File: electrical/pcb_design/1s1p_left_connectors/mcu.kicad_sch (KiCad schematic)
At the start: 14 parts, among them J17 STLINK_TagConnect_6, U1 BMI323, U2 BMI323, U4 STM32L452CEU6

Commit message: Verified schematics and PCBs for all boards
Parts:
- C1: footprint footprints:Nondescript_C_0603_1608Metric -> Capacitor_SMD:C_0603_1608Metric
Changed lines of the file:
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@@
       (effects (font (size 1.27 1.27)) (justify left))
     )
-    (property "Footprint" "footprints:Nondescript_C_0603_1608Metric" (at 24.13 121.92 0)
+    (property "Footprint" "Capacitor_SMD:C_0603_1608Metric" (at 24.13 121.92 0)
       (effects (font (size 1.27 1.27)) hide)
     )
@@
       (effects (font (size 1.27 1.27)) hide)
     )
-    (property "Datasheet" "https://octopart.com/datasheet/19-217%2Fbhc-zl1m2ry%2F3t-everlight-56007553" (at 170.18 135.89 0)
+    (property "Datasheet" "~" (at 170.18 135.89 0)
       (effects (font (size 1.27 1.27)) hide)
     )
@@
       (effects (font (size 1.27 1.27)) hide)
     )
-    (property "Datasheet" "https://www.bosch-sensortec.com/media/boschsensortec/downloads/datasheets/bst-bmi323-ds000.pdf" (at 83.82 16.51 0)
+    (property "Datasheet" "https://www.bosch-sensortec.com/media/boschsensortec/downloads/datasheets/bst-bmi160-ds000.pdf" (at 83.82 16.51 0)
       (effects (font (size 1.27 1.27)) hide)
     )
@@
       (effects (font (size 1.27 1.27)) hide)
     )
-    (property "Datasheet" "https://www.bosch-sensortec.com/media/boschsensortec/downloads/datasheets/bst-bmi323-ds000.pdf" (at 31.75 16.51 0)
-      (effects (font (size 1.27 1.27)) hide)
-    )
+    (property "Datasheet" "https://www.bosch-sensortec.com/media/boschsensortec/downloads/datasheets/bst-bmi160-ds000.pdf" (at 31.75 16.51 0)
+      (effects (font (size 1.27 1.27)) hide)
+    )

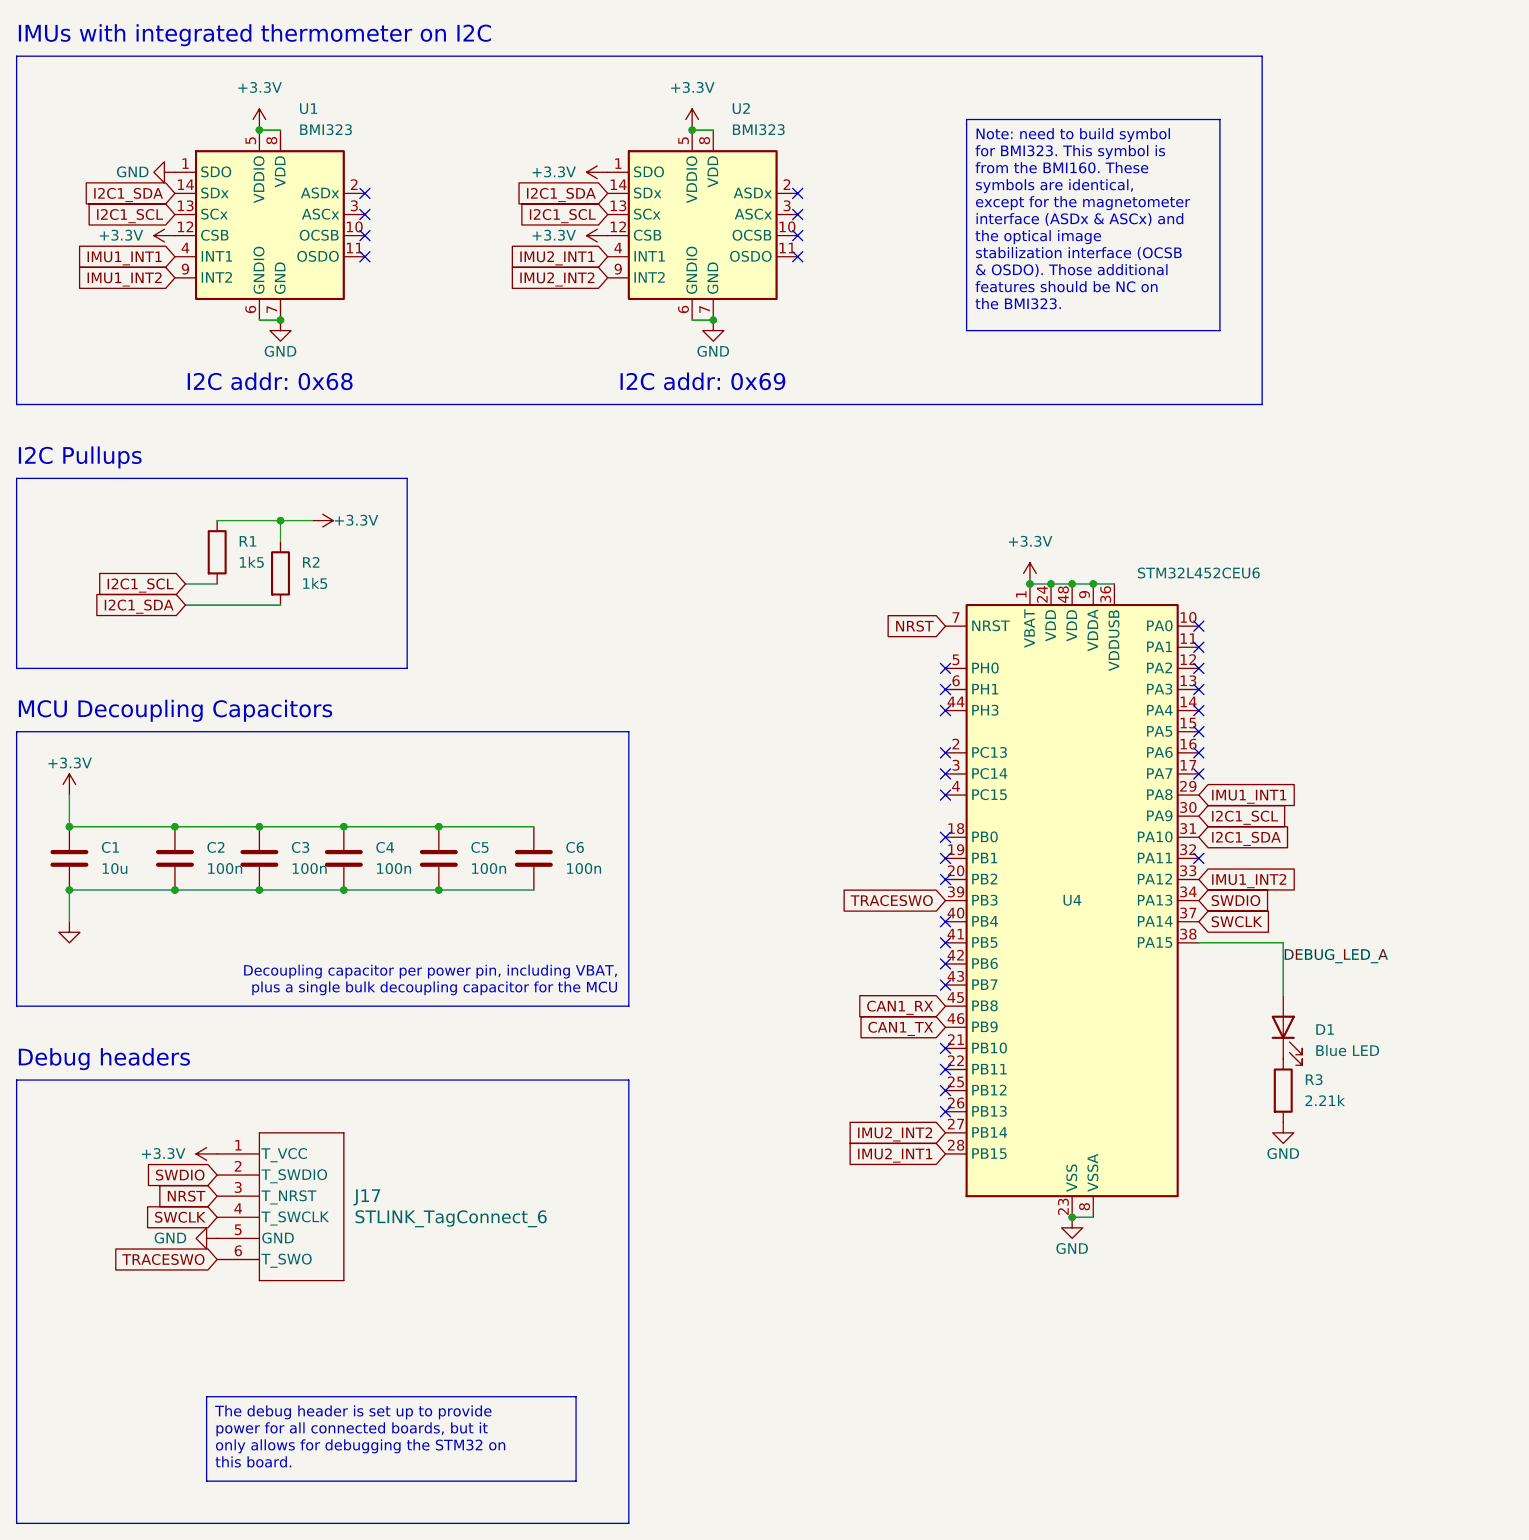
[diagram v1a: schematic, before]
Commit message: Added board identification mechanism. Updated production files and 3D models.
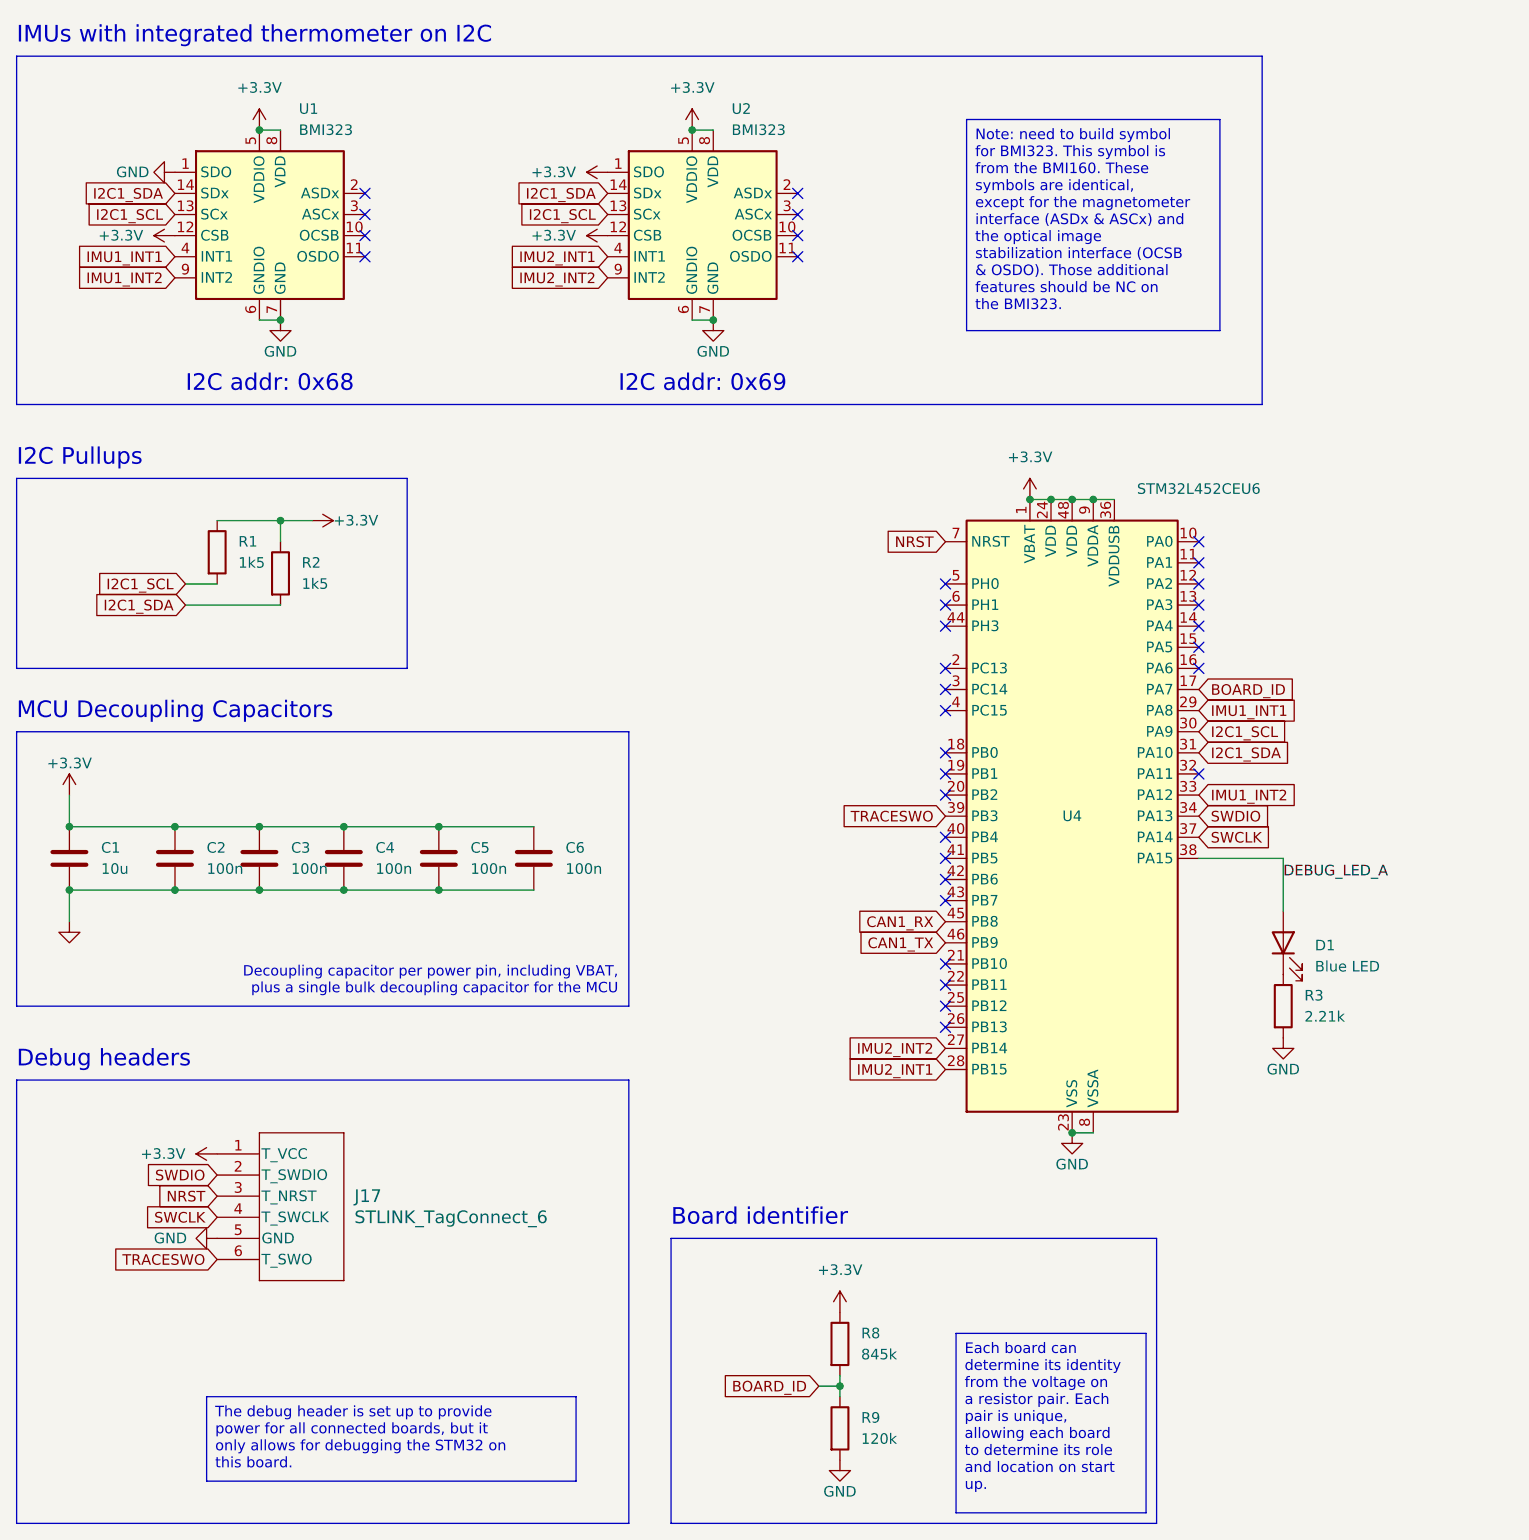
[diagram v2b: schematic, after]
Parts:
- added R8: 845k, footprints:Nondescript_R_0402_1005Metric, symbol Device:R
- added R9: 120k, footprints:Nondescript_R_0402_1005Metric, symbol Device:R
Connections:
- net +3.3V: now also R8.1
- net GND: now also R9.2
- net BOARD_ID: now reaches U4.17 (PA7)
- net BOARD_ID: now also R8.2, R9.1
- no-connect marks 34 -> 33
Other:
- note added: "Board identifier"
- moved on the sheet: D1, R3, U4

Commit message: Modified PCB designs to use local footprint for the STM32L452CEU6 part in order to configure the 3D model for this part.
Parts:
- U4: footprint Package_DFN_QFN:QFN-48-1EP_7x7mm_P0.5mm_EP5.6x5.6mm -> footprints:QFN-48-1EP_7x7mm_P0.5mm_EP5.6x5.6mm_ThermalVias
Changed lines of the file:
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@@
       (effects (font (size 1.27 1.27)) (justify left) hide)
     )
-    (property "Footprint" "Package_DFN_QFN:QFN-48-1EP_7x7mm_P0.5mm_EP5.6x5.6mm" (at 132.08 146.05 0)
+    (property "Footprint" "footprints:QFN-48-1EP_7x7mm_P0.5mm_EP5.6x5.6mm_ThermalVias" (at 132.08 146.05 0)
       (effects (font (size 1.27 1.27)) (justify right) hide)
     )

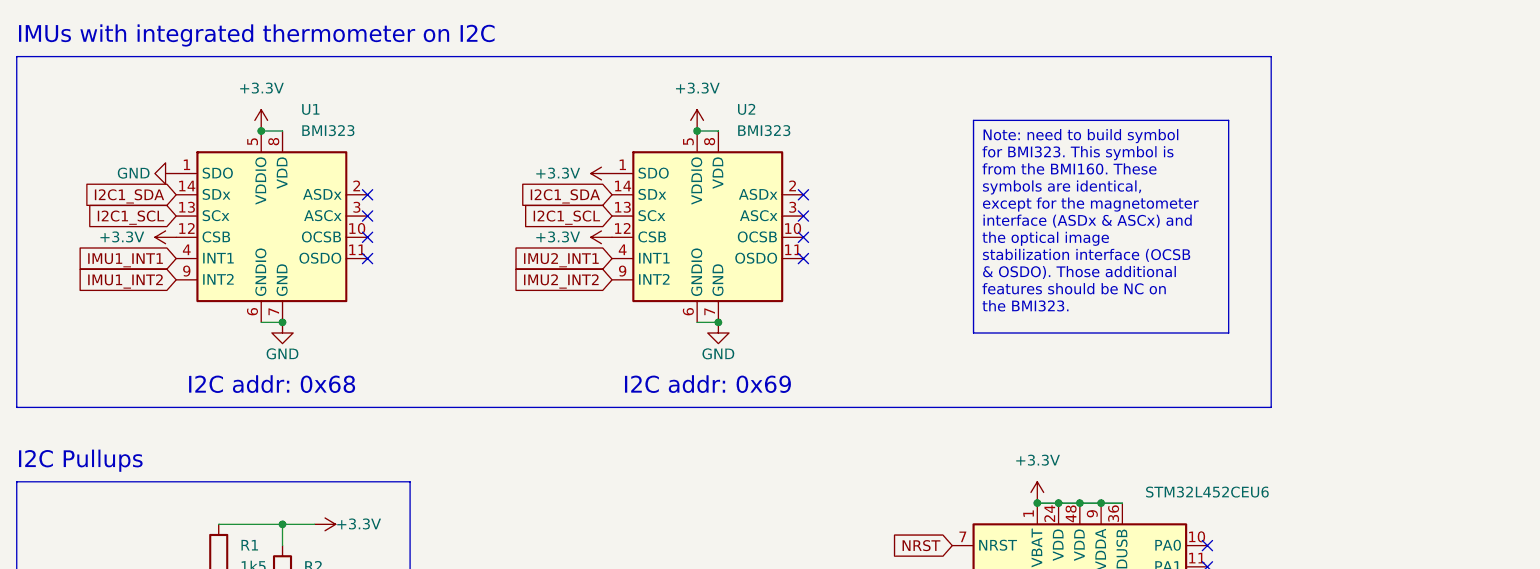
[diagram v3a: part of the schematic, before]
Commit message: Added decoupling capacitors for IMUs on battery boards
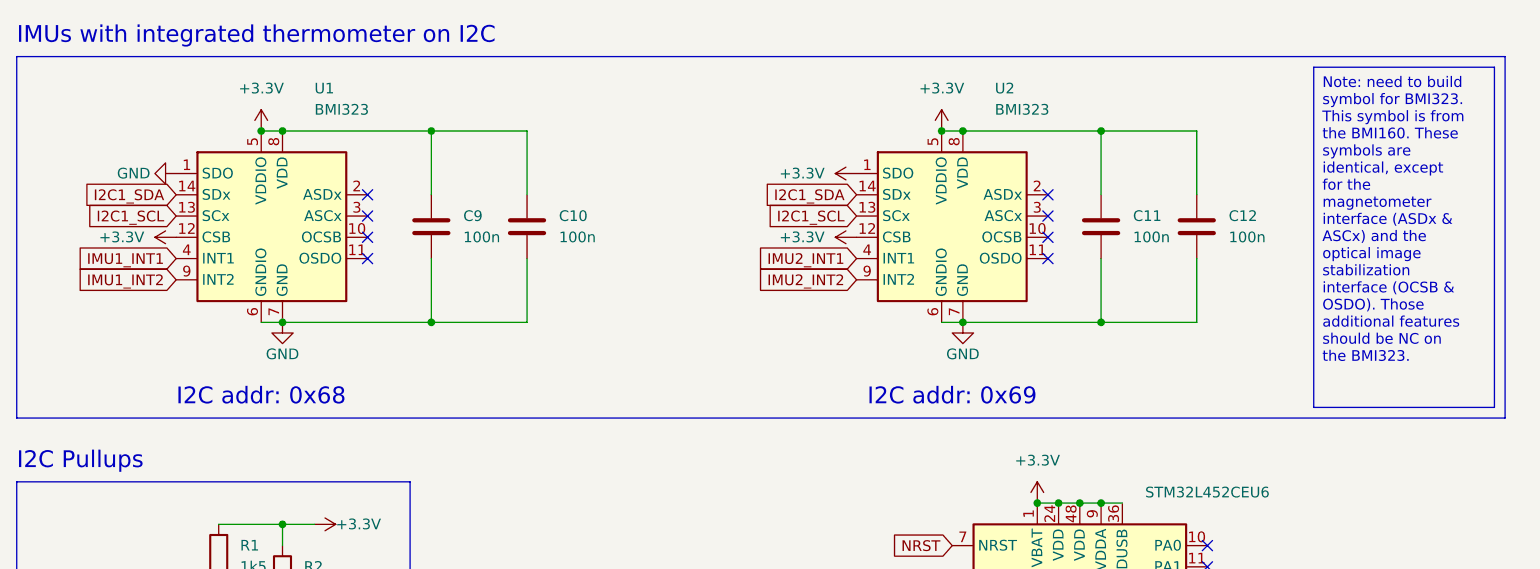
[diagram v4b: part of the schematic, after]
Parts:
- added C10, C11, C12, C9: 100n, footprints:Nondescript_C_0402_1005Metric, symbol TVSC:Small_Decoupling_Capacitor
- U1, U2: Tmax (none) -> 85; Tmin (none) -> -40; Tsensitivity (none) -> 2%
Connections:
- net +3.3V: now also C10.1, C11.1, C12.1, C9.1
- net GND: now also C10.2, C11.2, C12.2, C9.2
